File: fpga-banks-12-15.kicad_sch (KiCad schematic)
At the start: 1 part, among them U15 XC7K160T-FFG676

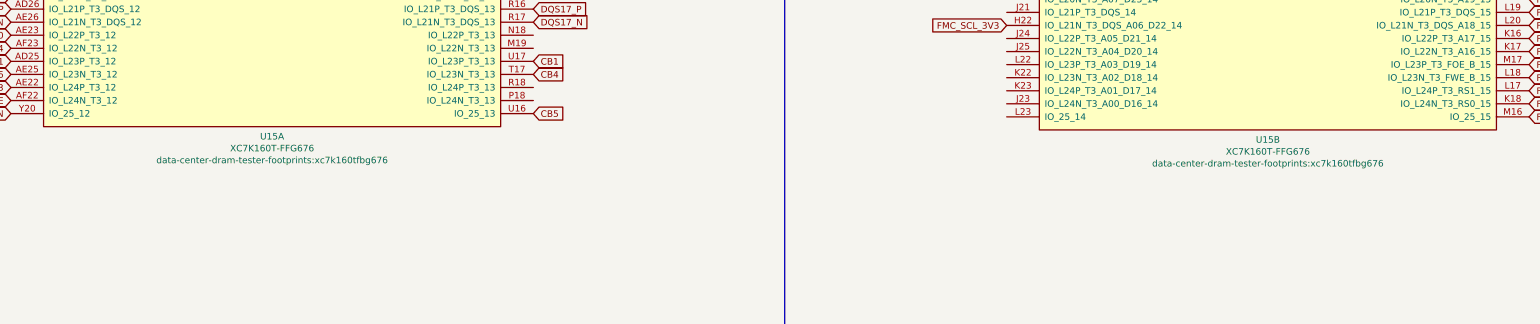
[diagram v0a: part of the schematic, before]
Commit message: Update PCB naming
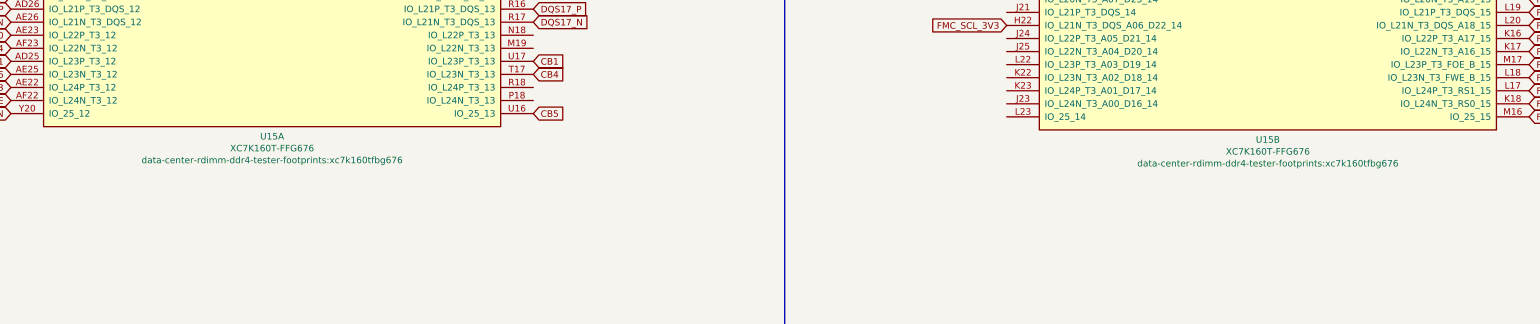
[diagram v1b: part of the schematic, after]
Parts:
- U15: footprint data-center-dram-tester-footprints:xc7k160tfbg676 -> data-center-rdimm-ddr4-tester-footprints:xc7k160tfbg676; symbol data-center-dram-tester:XC7K160T-FFG676 -> data-center-rdimm-ddr4-tester:XC7K160T-FFG676
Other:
- title: Data Center DRAM Tester -> Data Center RDIMM DDR4 Tester
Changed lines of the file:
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@@
   (paper "A3")
   (title_block
-    (title "Data Center DRAM Tester")
+    (title "Data Center RDIMM DDR4 Tester")
     (date "2023-02-01")
     (rev "1.2.1")
@@
     )
   )
-  (symbol (lib_id "data-center-dram-tester:XC7K160T-FFG676") (at 110.49 145.415 0) (unit 1)
+  (symbol (lib_id "data-center-rdimm-ddr4-tester:XC7K160T-FFG676") (at 110.49 145.415 0) (unit 1)
     (in_bom yes) (on_board yes)
     (property "Reference" "U15" (id 0) (at 110.49 220.98 0))
     (property "Value" "XC7K160T-FFG676" (id 1) (at 110.49 223.2914 0))
-    (property "Footprint" "data-center-dram-tester-footprints:xc7k160tfbg676" (id 2) (at 110.49 225.6028 0))
+    (property "Footprint" "data-center-rdimm-ddr4-tester-footprints:xc7k160tfbg676" (id 2) (at 110.49 225.6028 0))
     (property "Datasheet" "" (id 3) (at 110.49 145.415 0))
     (pin "AA21")
@@
     (pin "Y9")
   )
-  (symbol (lib_id "data-center-dram-tester:XC7K160T-FFG676") (at 304.165 146.05 0) (unit 2)
+  (symbol (lib_id "data-center-rdimm-ddr4-tester:XC7K160T-FFG676") (at 304.165 146.05 0) (unit 2)
     (in_bom yes) (on_board yes)
     (property "Reference" "U15" (id 0) (at 304.165 221.615 0))
     (property "Value" "XC7K160T-FFG676" (id 1) (at 304.165 223.9264 0))
-    (property "Footprint" "data-center-dram-tester-footprints:xc7k160tfbg676" (id 2) (at 304.165 226.2378 0))
+    (property "Footprint" "data-center-rdimm-ddr4-tester-footprints:xc7k160tfbg676" (id 2) (at 304.165 226.2378 0))
     (property "Datasheet" "" (id 3) (at 304.165 146.05 0))
     (pin "AA21")

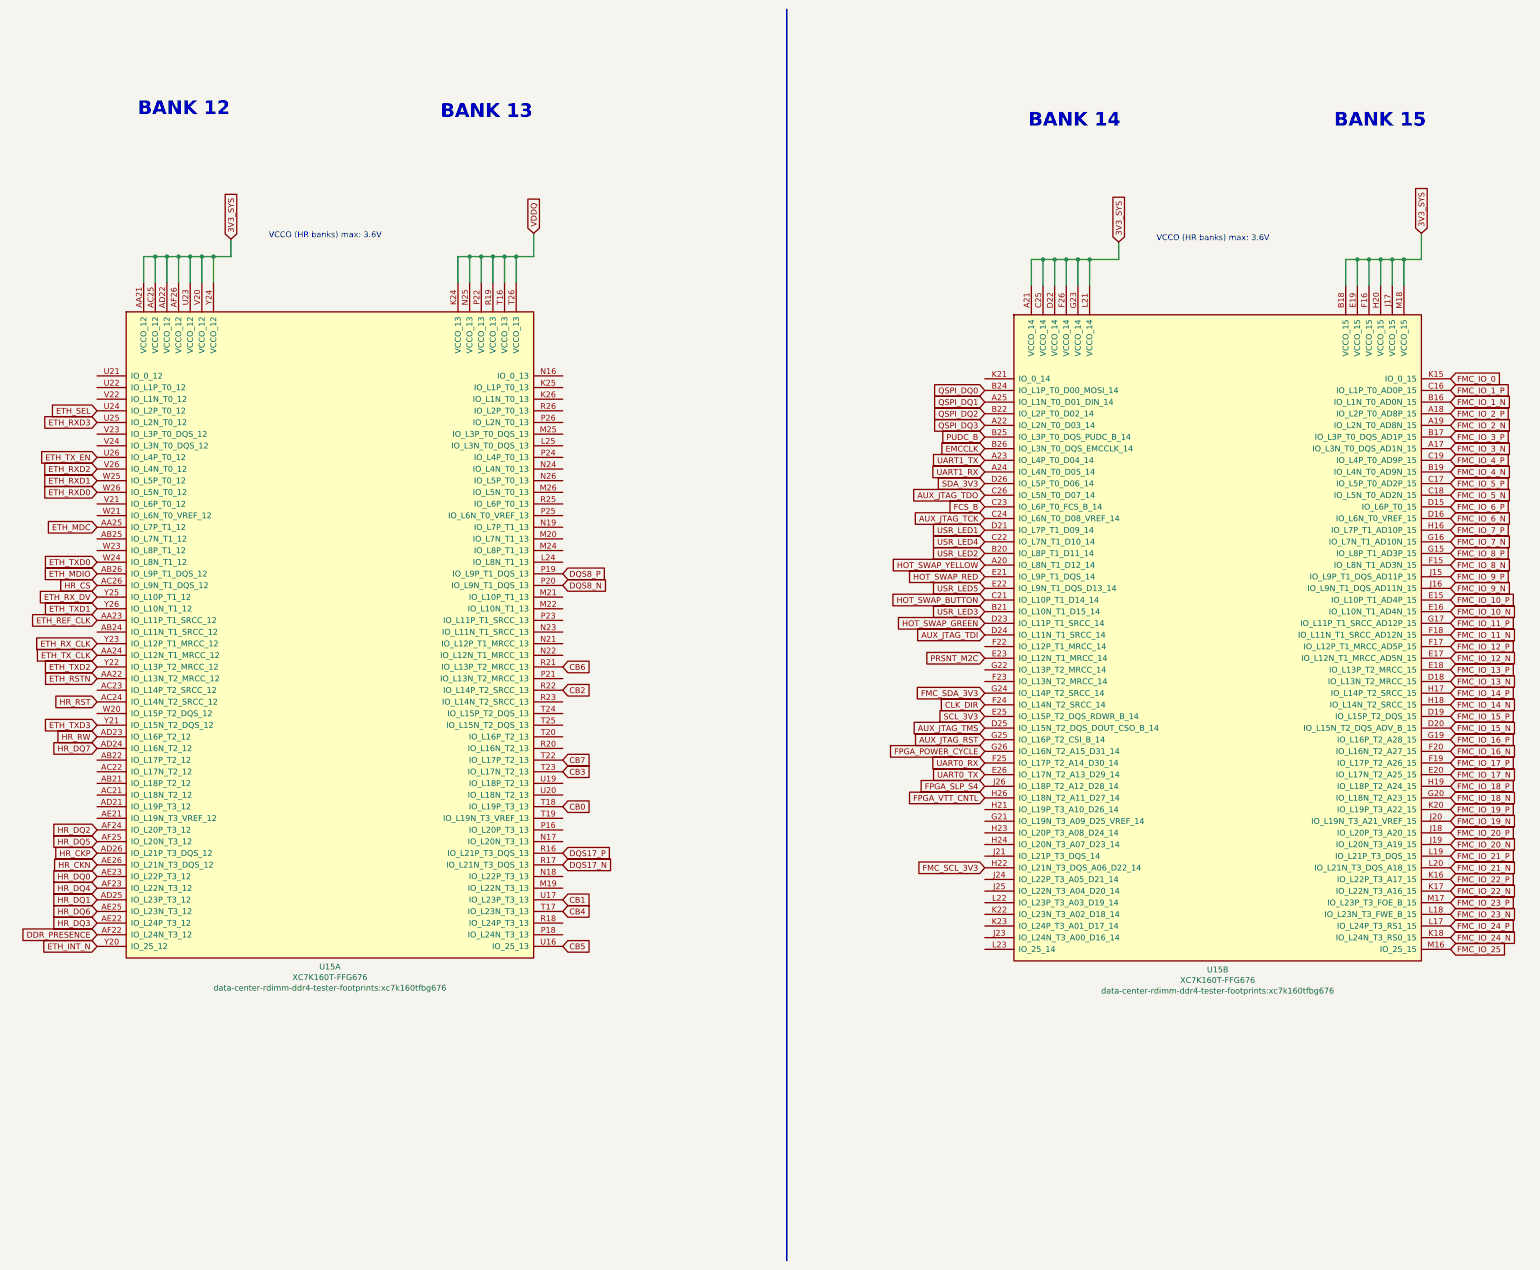
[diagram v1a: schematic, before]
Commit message: Introduce component standardization
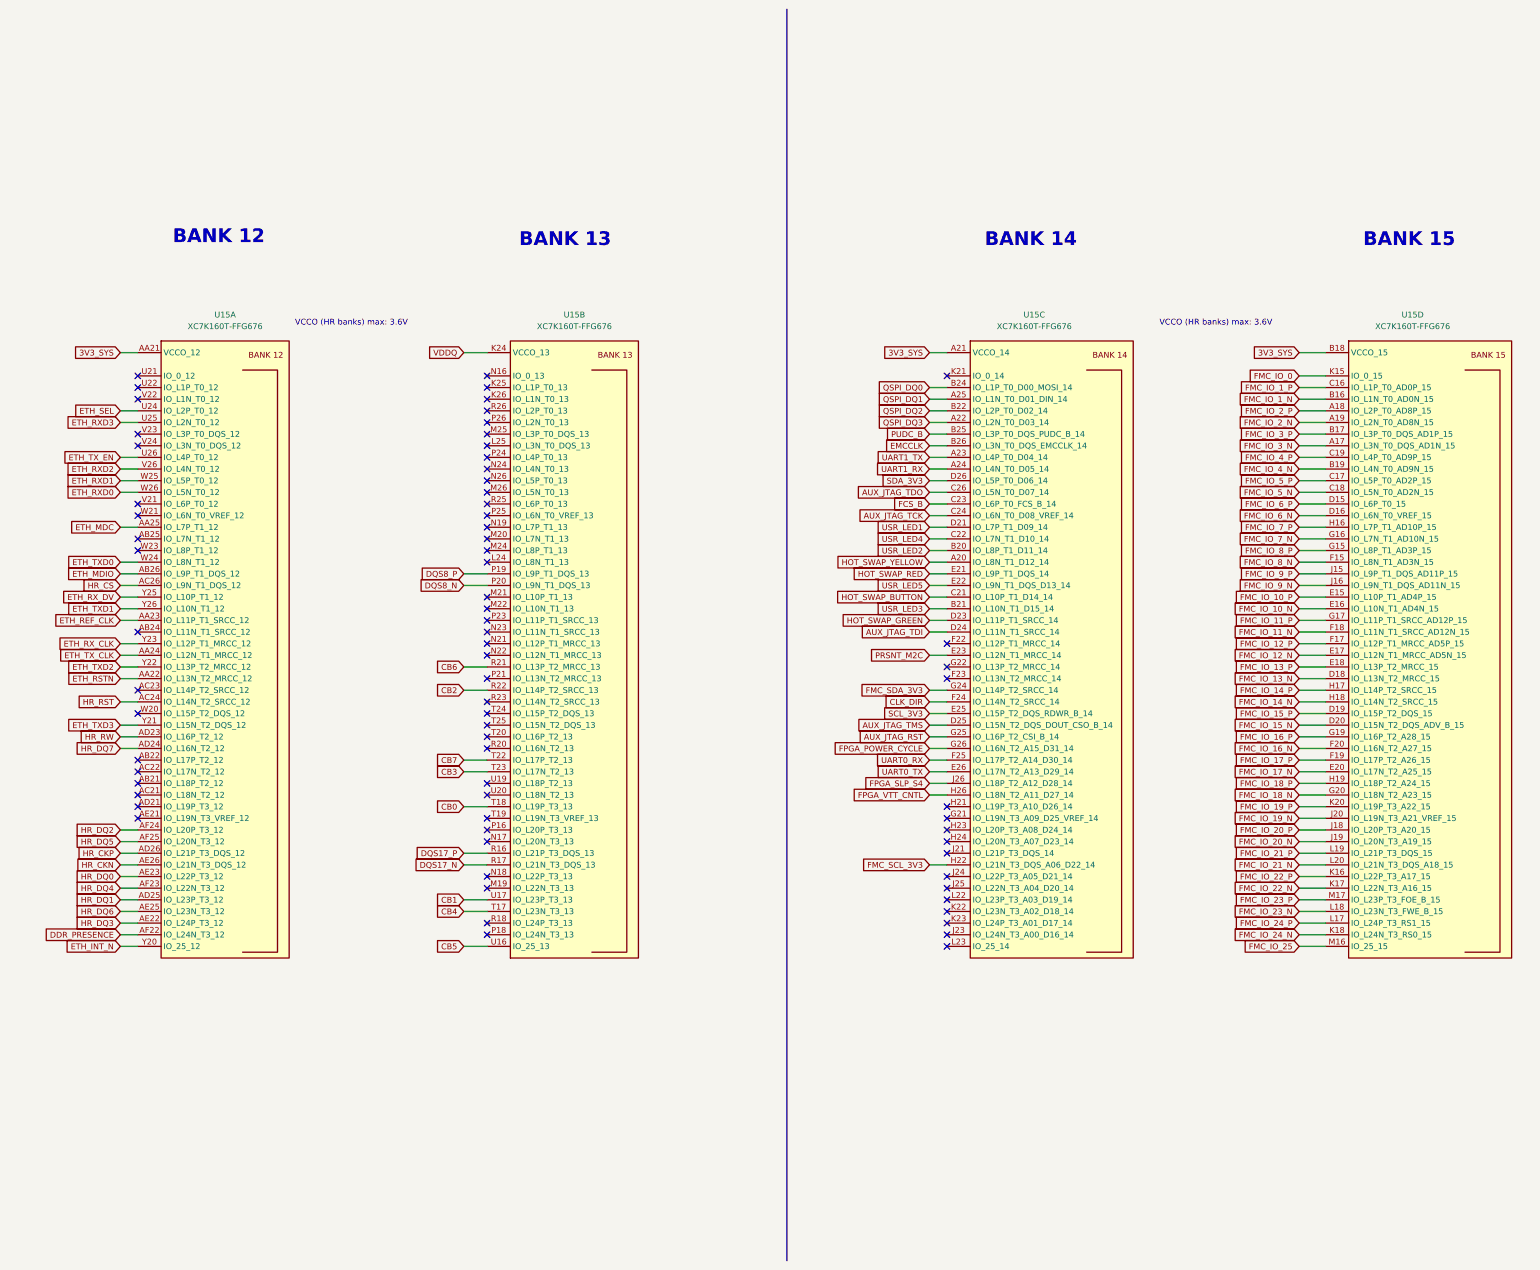
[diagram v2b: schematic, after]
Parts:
- added unit 4 of U15
- added unit 3 of U15
- U15: footprint data-center-rdimm-ddr4-tester-footprints:xc7k160tfbg676 -> data-center-rdimm-ddr4-tester-footprints:BGA-676_27x27mm_Layout26x26_P1X1mm; Author (none) -> Antmicro; License (none) -> Apache-2.0; MPN (none) -> XC7K160T-FFG676; Manufacturer (none) -> Xilinx
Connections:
- net 3V3_SYS: now also U15.A21 (VCCO_14), U15.B18 (VCCO_15), U15.C25 (VCCO_14), U15.D22 (VCCO_14), U15.E19 (VCCO_15), U15.F16 (VCCO_15), U15.F26 (VCCO_14), U15.G23 (VCCO_14), U15.H20 (VCCO_15), U15.J17 (VCCO_15), U15.L21 (VCCO_14), U15.M18 (VCCO_15); no longer U15.A21 (VCCO_14), U15.B18 (VCCO_15), U15.C25 (VCCO_14), U15.D22 (VCCO_14), U15.E19 (VCCO_15), U15.F16 (VCCO_15), U15.F26 (VCCO_14), U15.G23 (VCCO_14), U15.H20 (VCCO_15), U15.J17 (VCCO_15), U15.L21 (VCCO_14), U15.M18 (VCCO_15)
- net AUX_JTAG_RST: now also U15.G25 (IO_L16P_T2_CSI_B_14); no longer U15.G25 (IO_L16P_T2_CSI_B_14)
- net AUX_JTAG_TCK: now also U15.C24 (IO_L6N_T0_D08_VREF_14); no longer U15.C24 (IO_L6N_T0_D08_VREF_14)
- net AUX_JTAG_TDI: now also U15.D24 (IO_L11N_T1_SRCC_14); no longer U15.D24 (IO_L11N_T1_SRCC_14)
- net AUX_JTAG_TDO: now also U15.C26 (IO_L5N_T0_D07_14); no longer U15.C26 (IO_L5N_T0_D07_14)
- net AUX_JTAG_TMS: now also U15.D25 (IO_L15N_T2_DQS_DOUT_CSO_B_14); no longer U15.D25 (IO_L15N_T2_DQS_DOUT_CSO_B_14)
- net CB0: now also U15.T18 (IO_L19P_T3_13); no longer U15.T18 (IO_L19P_T3_13)
- net CB1: now also U15.U17 (IO_L23P_T3_13); no longer U15.U17 (IO_L23P_T3_13)
- net CB2: now also U15.R22 (IO_L14P_T2_SRCC_13); no longer U15.R22 (IO_L14P_T2_SRCC_13)
- net CB3: now also U15.T23 (IO_L17N_T2_13); no longer U15.T23 (IO_L17N_T2_13)
- net CB4: now also U15.T17 (IO_L23N_T3_13); no longer U15.T17 (IO_L23N_T3_13)
- net CB5: now also U15.U16 (IO_25_13); no longer U15.U16 (IO_25_13)
- net CB6: now also U15.R21 (IO_L13P_T2_MRCC_13); no longer U15.R21 (IO_L13P_T2_MRCC_13)
- net CB7: now also U15.T22 (IO_L17P_T2_13); no longer U15.T22 (IO_L17P_T2_13)
- net CLK_DIR: now also U15.F24 (IO_L14N_T2_SRCC_14); no longer U15.F24 (IO_L14N_T2_SRCC_14)
- net DQS17_N: now also U15.R17 (IO_L21N_T3_DQS_13); no longer U15.R17 (IO_L21N_T3_DQS_13)
- net DQS17_P: now also U15.R16 (IO_L21P_T3_DQS_13); no longer U15.R16 (IO_L21P_T3_DQS_13)
- net DQS8_N: now also U15.P20 (IO_L9N_T1_DQS_13); no longer U15.P20 (IO_L9N_T1_DQS_13)
- net DQS8_P: now also U15.P19 (IO_L9P_T1_DQS_13); no longer U15.P19 (IO_L9P_T1_DQS_13)
- net EMCCLK: now also U15.B26 (IO_L3N_T0_DQS_EMCCLK_14); no longer U15.B26 (IO_L3N_T0_DQS_EMCCLK_14)
- net FCS_B: now also U15.C23 (IO_L6P_T0_FCS_B_14); no longer U15.C23 (IO_L6P_T0_FCS_B_14)
- net FMC_IO_0: now also U15.K15 (IO_0_15); no longer U15.K15 (IO_0_15)
- net FMC_IO_10_N: now also U15.E16 (IO_L10N_T1_AD4N_15); no longer U15.E16 (IO_L10N_T1_AD4N_15)
- net FMC_IO_10_P: now also U15.E15 (IO_L10P_T1_AD4P_15); no longer U15.E15 (IO_L10P_T1_AD4P_15)
- net FMC_IO_11_N: now also U15.F18 (IO_L11N_T1_SRCC_AD12N_15); no longer U15.F18 (IO_L11N_T1_SRCC_AD12N_15)
- net FMC_IO_11_P: now also U15.G17 (IO_L11P_T1_SRCC_AD12P_15); no longer U15.G17 (IO_L11P_T1_SRCC_AD12P_15)
- net FMC_IO_12_N: now also U15.E17 (IO_L12N_T1_MRCC_AD5N_15); no longer U15.E17 (IO_L12N_T1_MRCC_AD5N_15)
- net FMC_IO_12_P: now also U15.F17 (IO_L12P_T1_MRCC_AD5P_15); no longer U15.F17 (IO_L12P_T1_MRCC_AD5P_15)
- net FMC_IO_13_N: now also U15.D18 (IO_L13N_T2_MRCC_15); no longer U15.D18 (IO_L13N_T2_MRCC_15)
- net FMC_IO_13_P: now also U15.E18 (IO_L13P_T2_MRCC_15); no longer U15.E18 (IO_L13P_T2_MRCC_15)
- net FMC_IO_14_N: now also U15.H18 (IO_L14N_T2_SRCC_15); no longer U15.H18 (IO_L14N_T2_SRCC_15)
- net FMC_IO_14_P: now also U15.H17 (IO_L14P_T2_SRCC_15); no longer U15.H17 (IO_L14P_T2_SRCC_15)
- net FMC_IO_15_N: now also U15.D20 (IO_L15N_T2_DQS_ADV_B_15); no longer U15.D20 (IO_L15N_T2_DQS_ADV_B_15)
- net FMC_IO_15_P: now also U15.D19 (IO_L15P_T2_DQS_15); no longer U15.D19 (IO_L15P_T2_DQS_15)
- net FMC_IO_16_N: now also U15.F20 (IO_L16N_T2_A27_15); no longer U15.F20 (IO_L16N_T2_A27_15)
- net FMC_IO_16_P: now also U15.G19 (IO_L16P_T2_A28_15); no longer U15.G19 (IO_L16P_T2_A28_15)
- net FMC_IO_17_N: now also U15.E20 (IO_L17N_T2_A25_15); no longer U15.E20 (IO_L17N_T2_A25_15)
- net FMC_IO_17_P: now also U15.F19 (IO_L17P_T2_A26_15); no longer U15.F19 (IO_L17P_T2_A26_15)
- net FMC_IO_18_N: now also U15.G20 (IO_L18N_T2_A23_15); no longer U15.G20 (IO_L18N_T2_A23_15)
- net FMC_IO_18_P: now also U15.H19 (IO_L18P_T2_A24_15); no longer U15.H19 (IO_L18P_T2_A24_15)
- net FMC_IO_19_N: now also U15.J20 (IO_L19N_T3_A21_VREF_15); no longer U15.J20 (IO_L19N_T3_A21_VREF_15)
- net FMC_IO_19_P: now also U15.K20 (IO_L19P_T3_A22_15); no longer U15.K20 (IO_L19P_T3_A22_15)
- net FMC_IO_1_N: now also U15.B16 (IO_L1N_T0_AD0N_15); no longer U15.B16 (IO_L1N_T0_AD0N_15)
- net FMC_IO_1_P: now also U15.C16 (IO_L1P_T0_AD0P_15); no longer U15.C16 (IO_L1P_T0_AD0P_15)
- net FMC_IO_20_N: now also U15.J19 (IO_L20N_T3_A19_15); no longer U15.J19 (IO_L20N_T3_A19_15)
- net FMC_IO_20_P: now also U15.J18 (IO_L20P_T3_A20_15); no longer U15.J18 (IO_L20P_T3_A20_15)
- net FMC_IO_21_N: now also U15.L20 (IO_L21N_T3_DQS_A18_15); no longer U15.L20 (IO_L21N_T3_DQS_A18_15)
- net FMC_IO_21_P: now also U15.L19 (IO_L21P_T3_DQS_15); no longer U15.L19 (IO_L21P_T3_DQS_15)
- net FMC_IO_22_N: now also U15.K17 (IO_L22N_T3_A16_15); no longer U15.K17 (IO_L22N_T3_A16_15)
- net FMC_IO_22_P: now also U15.K16 (IO_L22P_T3_A17_15); no longer U15.K16 (IO_L22P_T3_A17_15)
- net FMC_IO_23_N: now also U15.L18 (IO_L23N_T3_FWE_B_15); no longer U15.L18 (IO_L23N_T3_FWE_B_15)
- net FMC_IO_23_P: now also U15.M17 (IO_L23P_T3_FOE_B_15); no longer U15.M17 (IO_L23P_T3_FOE_B_15)
- net FMC_IO_24_N: now also U15.K18 (IO_L24N_T3_RS0_15); no longer U15.K18 (IO_L24N_T3_RS0_15)
- net FMC_IO_24_P: now also U15.L17 (IO_L24P_T3_RS1_15); no longer U15.L17 (IO_L24P_T3_RS1_15)
- net FMC_IO_25: now also U15.M16 (IO_25_15); no longer U15.M16 (IO_25_15)
- net FMC_IO_2_N: now also U15.A19 (IO_L2N_T0_AD8N_15); no longer U15.A19 (IO_L2N_T0_AD8N_15)
- net FMC_IO_2_P: now also U15.A18 (IO_L2P_T0_AD8P_15); no longer U15.A18 (IO_L2P_T0_AD8P_15)
- net FMC_IO_3_N: now also U15.A17 (IO_L3N_T0_DQS_AD1N_15); no longer U15.A17 (IO_L3N_T0_DQS_AD1N_15)
- net FMC_IO_3_P: now also U15.B17 (IO_L3P_T0_DQS_AD1P_15); no longer U15.B17 (IO_L3P_T0_DQS_AD1P_15)
- net FMC_IO_4_N: now also U15.B19 (IO_L4N_T0_AD9N_15); no longer U15.B19 (IO_L4N_T0_AD9N_15)
- net FMC_IO_4_P: now also U15.C19 (IO_L4P_T0_AD9P_15); no longer U15.C19 (IO_L4P_T0_AD9P_15)
- net FMC_IO_5_N: now also U15.C18 (IO_L5N_T0_AD2N_15); no longer U15.C18 (IO_L5N_T0_AD2N_15)
- net FMC_IO_5_P: now also U15.C17 (IO_L5P_T0_AD2P_15); no longer U15.C17 (IO_L5P_T0_AD2P_15)
- net FMC_IO_6_N: now also U15.D16 (IO_L6N_T0_VREF_15); no longer U15.D16 (IO_L6N_T0_VREF_15)
- net FMC_IO_6_P: now also U15.D15 (IO_L6P_T0_15); no longer U15.D15 (IO_L6P_T0_15)
- net FMC_IO_7_N: now also U15.G16 (IO_L7N_T1_AD10N_15); no longer U15.G16 (IO_L7N_T1_AD10N_15)
- net FMC_IO_7_P: now also U15.H16 (IO_L7P_T1_AD10P_15); no longer U15.H16 (IO_L7P_T1_AD10P_15)
- net FMC_IO_8_N: now also U15.F15 (IO_L8N_T1_AD3N_15); no longer U15.F15 (IO_L8N_T1_AD3N_15)
- net FMC_IO_8_P: now also U15.G15 (IO_L8P_T1_AD3P_15); no longer U15.G15 (IO_L8P_T1_AD3P_15)
- net FMC_IO_9_N: now also U15.J16 (IO_L9N_T1_DQS_AD11N_15); no longer U15.J16 (IO_L9N_T1_DQS_AD11N_15)
- net FMC_IO_9_P: now also U15.J15 (IO_L9P_T1_DQS_AD11P_15); no longer U15.J15 (IO_L9P_T1_DQS_AD11P_15)
- net FMC_SCL_3V3: now also U15.H22 (IO_L21N_T3_DQS_A06_D22_14); no longer U15.H22 (IO_L21N_T3_DQS_A06_D22_14)
- net FMC_SDA_3V3: now also U15.G24 (IO_L14P_T2_SRCC_14); no longer U15.G24 (IO_L14P_T2_SRCC_14)
- net FPGA_POWER_CYCLE: now also U15.G26 (IO_L16N_T2_A15_D31_14); no longer U15.G26 (IO_L16N_T2_A15_D31_14)
- net FPGA_SLP_S4: now also U15.J26 (IO_L18P_T2_A12_D28_14); no longer U15.J26 (IO_L18P_T2_A12_D28_14)
- net FPGA_VTT_CNTL: now also U15.H26 (IO_L18N_T2_A11_D27_14); no longer U15.H26 (IO_L18N_T2_A11_D27_14)
- net HOT_SWAP_BUTTON: now also U15.C21 (IO_L10P_T1_D14_14); no longer U15.C21 (IO_L10P_T1_D14_14)
- net HOT_SWAP_GREEN: now also U15.D23 (IO_L11P_T1_SRCC_14); no longer U15.D23 (IO_L11P_T1_SRCC_14)
- net HOT_SWAP_RED: now also U15.E21 (IO_L9P_T1_DQS_14); no longer U15.E21 (IO_L9P_T1_DQS_14)
- net HOT_SWAP_YELLOW: now also U15.A20 (IO_L8N_T1_D12_14); no longer U15.A20 (IO_L8N_T1_D12_14)
- net PRSNT_M2C: now also U15.E23 (IO_L12N_T1_MRCC_14); no longer U15.E23 (IO_L12N_T1_MRCC_14)
- net PUDC_B: now also U15.B25 (IO_L3P_T0_DQS_PUDC_B_14); no longer U15.B25 (IO_L3P_T0_DQS_PUDC_B_14)
- net QSPI_DQ0: now also U15.B24 (IO_L1P_T0_D00_MOSI_14); no longer U15.B24 (IO_L1P_T0_D00_MOSI_14)
- net QSPI_DQ1: now also U15.A25 (IO_L1N_T0_D01_DIN_14); no longer U15.A25 (IO_L1N_T0_D01_DIN_14)
- net QSPI_DQ2: now also U15.B22 (IO_L2P_T0_D02_14); no longer U15.B22 (IO_L2P_T0_D02_14)
- net QSPI_DQ3: now also U15.A22 (IO_L2N_T0_D03_14); no longer U15.A22 (IO_L2N_T0_D03_14)
- net SCL_3V3: now also U15.E25 (IO_L15P_T2_DQS_RDWR_B_14); no longer U15.E25 (IO_L15P_T2_DQS_RDWR_B_14)
- net SDA_3V3: now also U15.D26 (IO_L5P_T0_D06_14); no longer U15.D26 (IO_L5P_T0_D06_14)
- net UART0_RX: now also U15.F25 (IO_L17P_T2_A14_D30_14); no longer U15.F25 (IO_L17P_T2_A14_D30_14)
- net UART0_TX: now also U15.E26 (IO_L17N_T2_A13_D29_14); no longer U15.E26 (IO_L17N_T2_A13_D29_14)
- net UART1_RX: now also U15.A24 (IO_L4N_T0_D05_14); no longer U15.A24 (IO_L4N_T0_D05_14)
- net UART1_TX: now also U15.A23 (IO_L4P_T0_D04_14); no longer U15.A23 (IO_L4P_T0_D04_14)
- net USR_LED1: now also U15.D21 (IO_L7P_T1_D09_14); no longer U15.D21 (IO_L7P_T1_D09_14)
- net USR_LED2: now also U15.B20 (IO_L8P_T1_D11_14); no longer U15.B20 (IO_L8P_T1_D11_14)
- net USR_LED3: now also U15.B21 (IO_L10N_T1_D15_14); no longer U15.B21 (IO_L10N_T1_D15_14)
- net USR_LED4: now also U15.C22 (IO_L7N_T1_D10_14); no longer U15.C22 (IO_L7N_T1_D10_14)
- net USR_LED5: now also U15.E22 (IO_L9N_T1_DQS_D13_14); no longer U15.E22 (IO_L9N_T1_DQS_D13_14)
- net VDDQ: now also U15.K24 (VCCO_13), U15.N25 (VCCO_13), U15.P22 (VCCO_13), U15.R19 (VCCO_13), U15.T16 (VCCO_13), U15.T26 (VCCO_13); no longer U15.K24 (VCCO_13), U15.N25 (VCCO_13), U15.P22 (VCCO_13), U15.R19 (VCCO_13), U15.T16 (VCCO_13), U15.T26 (VCCO_13)
- no-connect marks 0 -> 72

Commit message: [#55119] component update
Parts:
- U15: footprint data-center-rdimm-ddr4-tester-footprints:BGA-676_27x27mm_Layout26x26_P1X1mm -> antmicro-footprints:BGA-676_27x27mm_Layout26x26_P1X1mm; symbol data-center-rdimm-ddr4-tester:XC7K160T-FFG676 -> antmicroMicrocontrollers:XC7K160T-FFG676; Manufacturer Xilinx -> AMD-Xilinx
